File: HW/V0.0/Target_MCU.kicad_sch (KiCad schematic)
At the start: 33 parts, among them J3 EXP PORT, U10 20MHz, U4 PIC16F877A

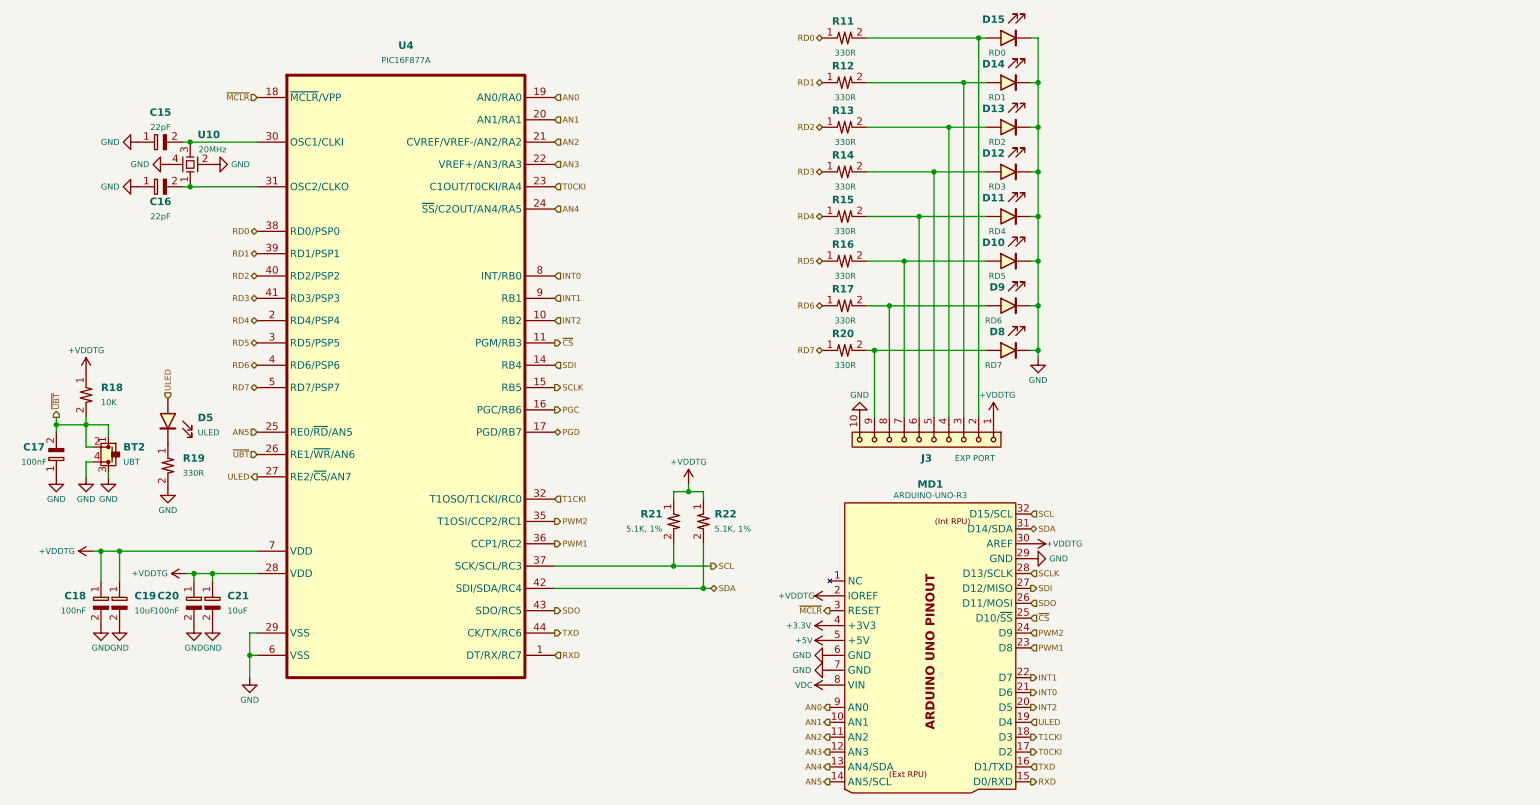
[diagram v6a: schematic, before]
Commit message: PIC16-DevKit-PCB-877 layout update 2
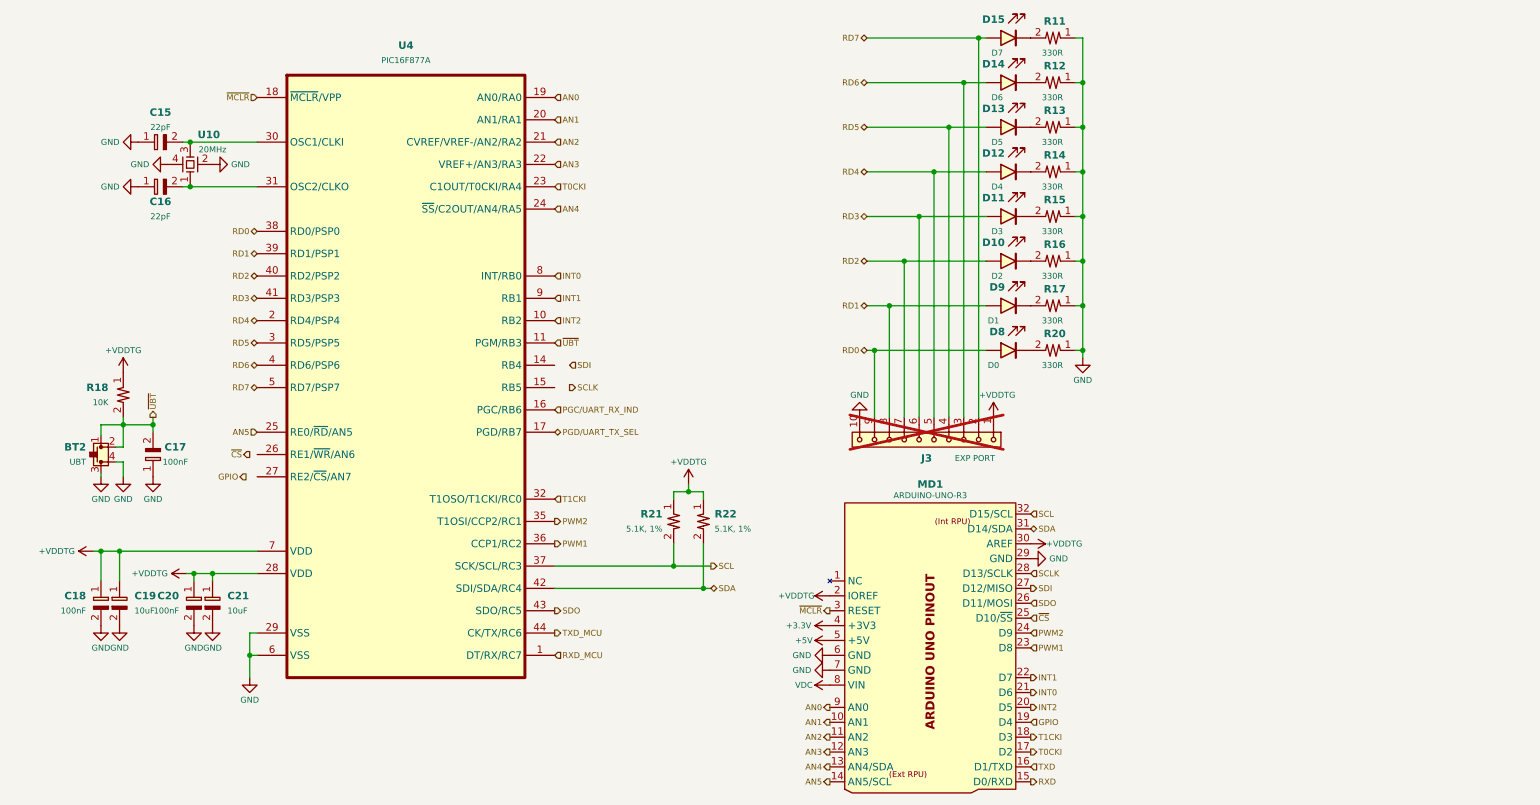
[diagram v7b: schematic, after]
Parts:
- removed D5: ULED, SAMPI:LED0603, symbol Triet_KiCAD_Sym:LED
- removed R19: 330R, SAMPI:RES0603, symbol Triet_KiCAD_Sym:RES
- D10: value RD5 -> D2
- D11: value RD4 -> D3
- D12: value RD3 -> D4
- D13: value RD2 -> D5
- D14: value RD1 -> D6
- D15: value RD0 -> D7
- D8: value RD7 -> D0
- D9: value RD6 -> D1
- J3: now not fitted; now left out of the parts list
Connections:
- net GND: now also R11.1, R12.1, R13.1, R14.1, R15.1, R16.1, R17.1, R20.1; no longer D10.K, D11.K, D12.K, D13.K, D14.K, D15.K, D8.K, D9.K
- net RD0: now also D8.A, J3.9; no longer R11.1
- net RD1: now also D9.A, J3.8; no longer R12.1
- net RD2: now also D10.A, J3.7; no longer R13.1
- net RD3: now also D11.A, J3.6; no longer R14.1
- net RD4: now also D12.A, J3.5; no longer R15.1
- net RD5: now also D13.A, J3.4; no longer R16.1
- net RD6: now also D14.A, J3.3; no longer R17.1
- net RD7: now also D15.A, J3.2; no longer R20.1
- net RXD: no longer U4.1 (DT/RX/RC7)
- net SCLK: no longer U4.15 (RB5)
- net SDI: no longer U4.14 (RB4)
- net TXD: no longer U4.44 (CK/TX/RC6)
- net ~{CS}: no longer U4.11 (PGM/RB3)
- net ~{UBT}: now also U4.11 (PGM/RB3); no longer U4.26 (RE1/~{WR}/AN6)
- net PGC renamed PGC/UART_RX_IND
- net PGD renamed PGD/UART_TX_SEL
- net ULED: no longer names the net of U4.27 (RE2/~{CS}/AN7)
- net ULED: no longer MD1.19 (D4)
- new net: D15.K, R11.2
- new net: D8.K, R20.2
- new net: D12.K, R14.2
- new net: D10.K, R16.2
- new net: D11.K, R15.2
- new net: D14.K, R12.2
- new net: D9.K, R17.2
- new net: D13.K, R13.2
- new net GPIO: MD1.19 (D4)
- new net RXD_MCU: U4.1 (DT/RX/RC7)
- new net TXD_MCU: U4.44 (CK/TX/RC6)
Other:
- moved on the sheet: BT2, C17, R11, R12, R13, R14, R15, R16, R17, R18, R20

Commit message: PIC16-DevKit-PCB-877 layout update 3: Add QWIIC port
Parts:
- added J5: QWIIC, SAMPI:HDM-1x4x1.0-RA, symbol SAMPI:QWIIC
- added Q6, Q7: SI2302, SAMPI:SOT23, symbol SAMPI:FET_N-CH
- added R28, R30: 5.1K, 1%, SAMPI:RES0603, symbol Triet_KiCAD_Sym:RES
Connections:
- net +3.3V: now also J5.2 (VDD), Q6.1 (G), Q7.1 (G), R28.1, R30.1
- net GND: now also J5.0 (EP), J5.1 (GND)
- net SCL: now also R22.2, Q6.3 (D); no longer R21.2
- net SDA: now also R21.2, Q7.3 (D); no longer R22.2
- new net: J5.4 (SCL), Q6.2 (S), R28.2
- new net: J5.3 (SDA), Q7.2 (S), R30.2
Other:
- moved on the sheet: R21, R22
